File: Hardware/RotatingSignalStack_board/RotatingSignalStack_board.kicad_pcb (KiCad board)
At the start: 2 copper layers, 81.3 x 71.1 mm, 30 parts, among them J1 8P8C_LED_Shielded, J2 Conn_01x05_Pin, SW1 SW_Push, SW2 SW_Push, U1 OKI, U3 Teensy4.1_DEV-16771

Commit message: first layout commit - lots of expected changes
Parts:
- moved R3 32.0 mm to (144.8, 47.0)
- moved R4 32.0 mm to (142.2, 47.0)
- moved C4 17.4 mm to (149.5, 104.1)
- moved C5 17.4 mm to (149.5, 106.7)
- moved C3 17.4 mm to (149.5, 101.6)
- moved U3 7.62 mm to (142.2, 61.0)
- moved J1 6.48 mm to (190.8, 86.9)
- moved C6 3.02 mm to (159.2, 90.2), turned to 180 degrees
- moved R1 2.54 mm to (137.2, 81.3)
- moved D1 2.54 mm to (137.2, 83.8)
- moved J2 2.27 mm to (169.4, 45.7)
- moved Conn5 1.27 mm to (139.7, 74.9)
- moved C1 1.27 mm to (137.2, 87.6)
- moved V2 0.12 mm to (178.9, 49.7)
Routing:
- net +3.3V: track 0.00 -> 145.2 mm, vias 0 -> 4
- net /Tx-: track 0.00 -> 95.0 mm
- net /Tx+: track 0.00 -> 94.8 mm
- net /Rx+: track 0.00 -> 85.0 mm
- net /Rx-: track 0.00 -> 84.8 mm
- net +12V: track 0.00 -> 83.9 mm, vias 0 -> 2
- net /LED: track 0.00 -> 77.1 mm, vias 0 -> 4
- net JOG B: track 0.00 -> 68.6 mm, vias 0 -> 2
- net JOG A: track 0.00 -> 63.6 mm, vias 0 -> 1
- net I2C SCL: track 0.00 -> 54.2 mm, vias 0 -> 1
- net COMP PWR: track 0.00 -> 54.1 mm, vias 0 -> 1
- net I2C SDA: track 0.00 -> 52.6 mm
- net MAG ENABLE: track 0.00 -> 37.7 mm, vias 0 -> 1
- net Net-(C6-Pad1): track 0.00 -> 13.8 mm
- net GND: track 0.00 -> 9.77 mm, vias 0 -> 20
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- added copper zone on B.Cu, net GND
- added copper zone on F.Cu, net GND
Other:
- board size 81.3 x 71.1 mm -> 84.3 x 74.1 mm
- board text added: "COMPASS"
- board text added: "H-BRIDGE"
- board text added: "L"
- board text added: "MOTOR OUT"
- board text added: "PWR IN"
- board text added: "R"
- board text added: "TyTyTheToeH"

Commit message: changes layout reveiw 1
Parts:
- removed Conn5: Molex_SL_04, MRDT_Connectors:MOLEX_SL_04_Vertical
- added Conn1: Molex_SL_03, MRDT_Connectors:MOLEX_SL_03_Vertical, F.Cu at (159.4, 147.6)
- added R5: 0, Jumper:SolderJumper-2_P1.3mm_Open_RoundedPad1.0x1.5mm, B.Cu at (150.2, 104.9)
- Conn2, Conn3: moved to F.Cu
- J2: footprint Connector_PinHeader_1.00mm:PinHeader_1x05_P1.00mm_Vertical -> Connector_PinHeader_2.54mm:PinHeader_1x05_P2.54mm_Vertical
- moved R4 104.9 mm to (165.1, 149.4), turned to 90 degrees
- moved R3 100.4 mm to (165.1, 145.3), turned to 90 degrees
- moved Conn6 93.2 mm to (162.1, 138.9)
- moved J2 88.1 mm to (151.9, 132.1)
- moved SW1 84.6 mm to (178.3, 134.1)
- moved SW2 84.6 mm to (172.2, 134.1)
- moved R13 80.9 mm to (171.7, 140.7)
- moved R18 80.9 mm to (169.2, 140.7)
- moved D14 80.0 mm to (169.2, 144.4), turned to 90 degrees
- moved D13 80.0 mm to (171.7, 144.4), turned to 90 degrees
- moved V1 75.7 mm to (173.7, 91.8), turned to 0 degrees
- moved V2 71.8 mm to (120.6, 91.8), turned to 90 degrees
- moved R1 67.2 mm to (126.2, 147.5)
- moved D1 64.2 mm to (129.9, 147.6), turned to 180 degrees
- moved C1 61.9 mm to (146.4, 148.8), turned to -90 degrees
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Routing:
- net /Rx+: track 85.0 -> 44.4 mm
- net /Rx-: track 84.8 -> 44.3 mm
- net HB_FWD: track 8.98 -> 48.8 mm, vias 0 -> 1
- net /Tx-: track 95.0 -> 55.8 mm
- net /Tx+: track 94.8 -> 55.8 mm
- net HB_RVS: track 8.98 -> 47.3 mm, vias 0 -> 1
- net +12V: track 83.9 -> 54.4 mm
- net COMP PWR: track 54.1 -> 78.4 mm, vias 1 -> 2
- net I2C SCL: track 54.2 -> 78.2 mm, vias 1 -> 3
- net JOG B: track 68.6 -> 45.8 mm, vias 2 -> 1
- net MAG ENABLE: track 37.7 -> 59.2 mm
- net +3.3V: track 145.2 -> 165.1 mm, vias 4 -> 2
- net JOG A: track 63.6 -> 46.1 mm
- net /LED: track 77.1 -> 64.8 mm, vias 4 -> 0
- net I2C SDA: track 52.6 -> 64.1 mm, vias 0 -> 3
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- added copper zone on F.Cu, net +12V
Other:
- board size 84.3 x 74.1 mm -> 69.1 x 69 mm
- board text added: "12v"
- board text added: "3.3v"
- board text added: "3.3v Direct Pwr Compass"
- board text added: "IN"
- board text added: "OUT"
- board text added: "ROTATING SIGNAL STACK"
- board text removed: "MOTOR OUT"
- board text removed: "PWR IN"
- board text removed: "TyTyTheToeH"

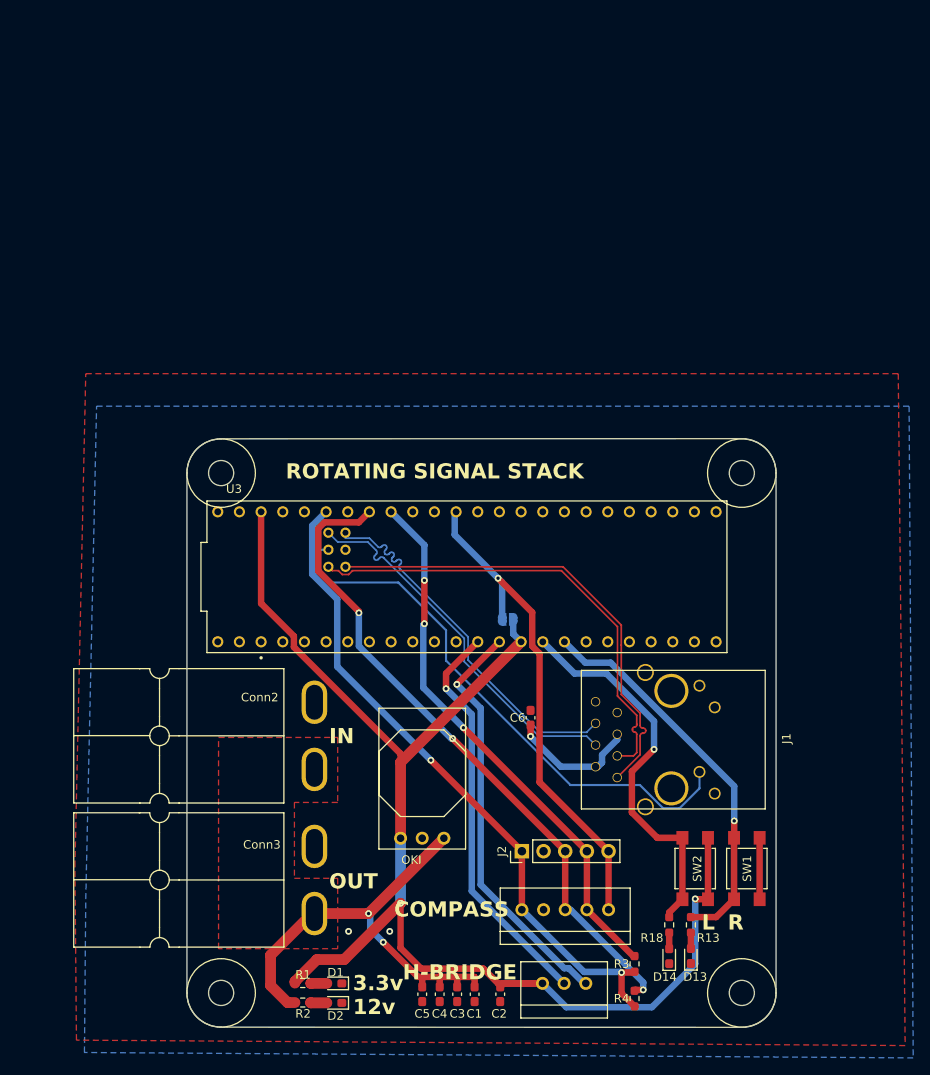
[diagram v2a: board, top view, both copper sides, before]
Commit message: layout changes- diff pair length, moved labels, trace width changed, OKI capacitors moved, x
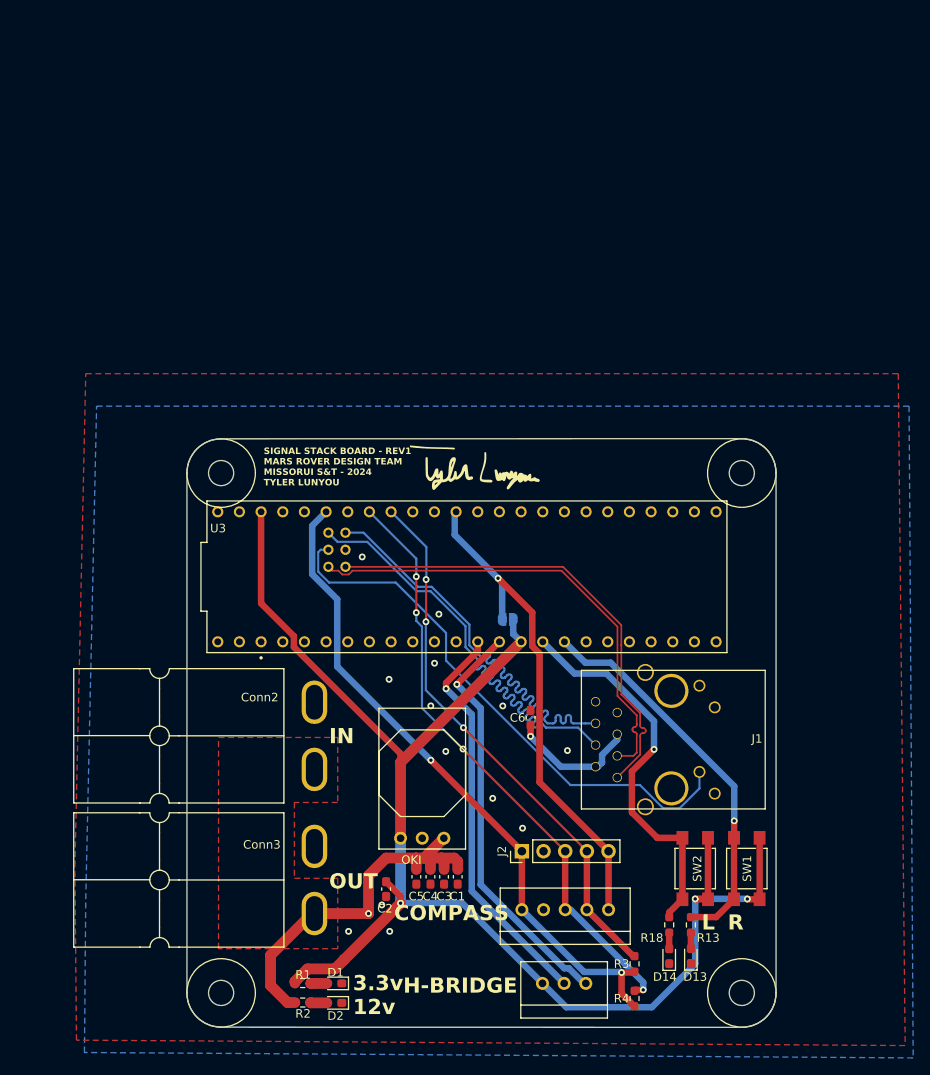
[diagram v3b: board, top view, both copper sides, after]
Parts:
- added G***: LOGO, MRDT_Silkscreens:z_sig_Tyler_Lunyou_Sig_30mmx7, F.Cu at (151.2, 87.1)
- moved C2 18.2 mm to (136.0, 136.5)
- moved C1 13.9 mm to (144.4, 135.1)
- moved C3 13.8 mm to (142.8, 135.1)
- moved C4 13.8 mm to (141.2, 135.1)
- moved C5 13.8 mm to (139.5, 135.1)
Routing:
- net /Rx+: track 44.4 -> 55.4 mm
- net /Rx-: track 44.3 -> 55.4 mm
- net +12V: track 54.4 -> 45.1 mm, vias 2 -> 1
- net I2C SCL: track 78.2 -> 70.8 mm, vias 3 -> 4
- net +3.3V: track 165.1 -> 168.1 mm, vias 2 -> 3
- net GND: vias 2 -> 13
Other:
- board text added: "3.3v Direct Power Compass"
- board text added: "SIGNAL STACK BOARD - REV1 MARS ROVER DESIGN TEAM MISSORUI S&T - 2024 TYLER LUNYOU"
- board text removed: "3.3v Direct Pwr Compass"
- board text removed: "ROTATING SIGNAL STACK"

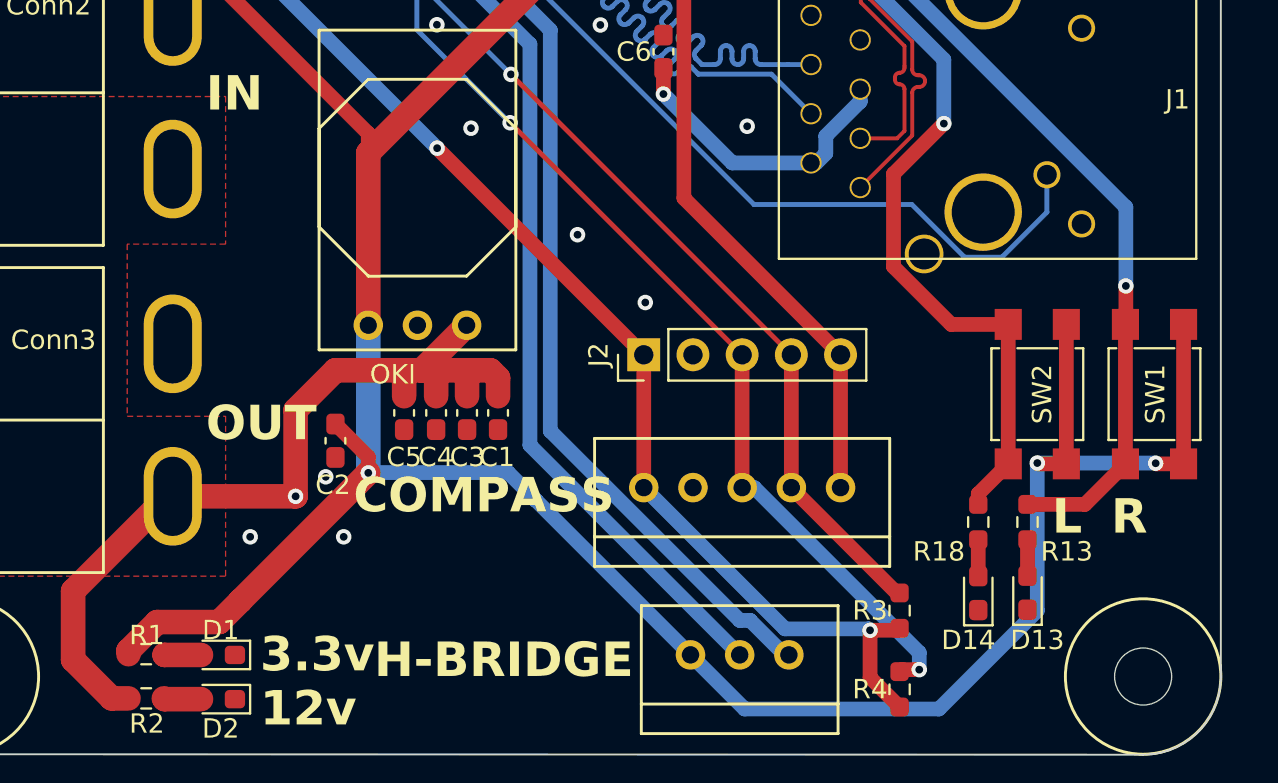
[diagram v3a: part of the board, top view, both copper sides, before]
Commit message: layout changes- diff pair length, moved labels, trace width changed, OKI capacitors moved, x
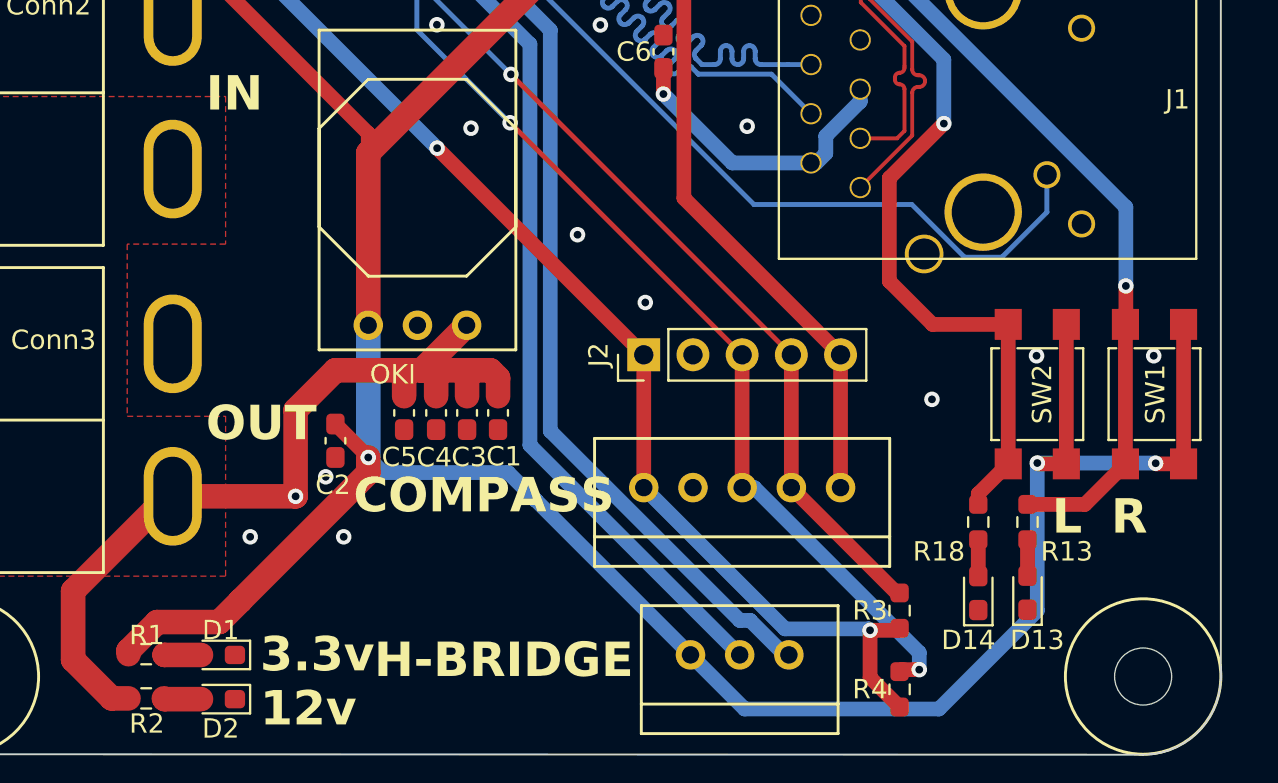
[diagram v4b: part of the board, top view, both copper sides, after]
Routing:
- net JOG B: track 45.8 -> 46.5 mm
- net GND: vias 13 -> 16
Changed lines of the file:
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@@
     (property "ki_keywords" "cap capacitor")
     (attr smd)
-    (fp_text reference "C1" (at 2.286 0.050625 -180) (layer "F.SilkS")
+    (fp_text reference "C1" (at 2.25 -0.30225 -180) (layer "F.SilkS")
         (effects (font (size 1 1) (thickness 0.15)))
     )
@@
     (property "ki_keywords" "cap capacitor")
     (attr smd)
-    (fp_text reference "C4" (at 2.286 0.016875 -180) (layer "F.SilkS")
+    (fp_text reference "C4" (at 2.3 0.1 -180) (layer "F.SilkS")
         (effects (font (size 1 1) (thickness 0.15)))
     )
@@
     (property "ki_keywords" "cap capacitor")
     (attr smd)
-    (fp_text reference "C3" (at 2.286 -0.016875 -180) (layer "F.SilkS")
+    (fp_text reference "C3" (at 2.286 -0.10225 -180) (layer "F.SilkS")
         (effects (font (size 1 1) (thickness 0.15)))
     )
@@
     (property "ki_keywords" "cap capacitor")
     (attr smd)
-    (fp_text reference "C5" (at 2.286 0) (layer "F.SilkS")
+    (fp_text reference "C5" (at 2.286 0.24775) (layer "F.SilkS")
         (effects (font (size 1 1) (thickness 0.15)))
     )
@@
   (via (at 131.572 141.478) (size 0.8) (drill 0.4) (layers "F.Cu" "B.Cu") (free) (net 2))
   (via (at 151.972 129.38) (size 0.8) (drill 0.4) (layers "F.Cu" "B.Cu") (free) (net 2))
+  (via (at 172.172 132.13) (size 0.8) (drill 0.4) (layers "F.Cu" "B.Cu") (free) (net 2))
   (via (at 142.972 120.38) (size 0.8) (drill 0.4) (layers "F.Cu" "B.Cu") (free) (net 2))
   (via (at 149.652 115.05) (size 0.8) (drill 0.4) (layers "F.Cu" "B.Cu") (free) (net 2))
   (via (at 142.162 104.29) (size 0.8) (drill 0.4) (layers "F.Cu" "B.Cu") (free) (net 2))
+  (via (at 166.772 134.38) (size 0.8) (drill 0.4) (layers "F.Cu" "B.Cu") (free) (net 2))
   (via (at 136.322 111.93) (size 0.8) (drill 0.4) (layers "F.Cu" "B.Cu") (free) (net 2))
   (via (at 141.212 115.04) (size 0.8) (drill 0.4) (layers "F.Cu" "B.Cu") (free) (net 2))
@@
   (via (at 148.472 125.88) (size 0.8) (drill 0.4) (layers "F.Cu" "B.Cu") (free) (net 2))
   (via (at 157.232 120.28) (size 0.8) (drill 0.4) (layers "F.Cu" "B.Cu") (free) (net 2))
+  (via (at 178.222 132.13) (size 0.8) (drill 0.4) (layers "F.Cu" "B.Cu") (free) (net 2))
   (segment (start 173.712 130.512) (end 173.712 137.712) (width 0.762) (layer "F.Cu") (net 3))
-  (segment (start 135.972 135.655) (end 137.668 137.351) (width 0.762) (layer "F.Cu") (net 3))
+  (segment (start 125.288 147.358256) (end 125.288 147.5375) (width 1.27) (layer "F.Cu") (net 3))
+  (segment (start 137.668 137.38) (end 137.668 138.176) (width 1.27) (layer "F.Cu") (net 3))
   (segment (start 178.354 137.712) (end 178.322 137.68) (width 0.762) (layer "F.Cu") (net 3))
-  (segment (start 137.668 137.351) (end 137.668 138.176) (width 0.762) (layer "F.Cu") (net 3))
-  (segment (start 129.972 145.88) (end 131.064 144.788) (width 1.27) (layer "F.Cu") (net 3))
+  (segment (start 137.668 137.351) (end 135.972 135.655) (width 0.762) (layer "F.Cu") (net 3))
   (segment (start 179.762 137.712) (end 179.762 130.512) (width 0.762) (layer "F.Cu") (net 3))
+  (segment (start 137.668 138.176) (end 131.064 144.78) (width 1.27) (layer "F.Cu") (net 3))
+  (segment (start 131.064 144.788) (end 129.972 145.88) (width 1.27) (layer "F.Cu") (net 3))
   (segment (start 179.762 137.712) (end 178.354 137.712) (width 0.762) (layer "F.Cu") (net 3))
   (segment (start 173.712 137.712) (end 172.256 137.712) (width 0.762) (layer "F.Cu") (net 3))
-  (segment (start 131.064 144.788) (end 131.064 144.78) (width 1.27) (layer "F.Cu") (net 3))
-  (segment (start 131.064 144.78) (end 137.668 138.176) (width 1.27) (layer "F.Cu") (net 3))
   (segment (start 172.256 137.712) (end 172.212 137.668) (width 0.762) (layer "F.Cu") (net 3))
-  (segment (start 125.288 147.5375) (end 125.288 147.358256) (width 1.27) (layer "F.Cu") (net 3))
   (segment (start 137.668 121.66) (end 151.799 107.529) (width 1.27) (layer "F.Cu") (net 3))
-  (segment (start 126.766256 145.88) (end 129.972 145.88) (width 1.27) (layer "F.Cu") (net 3))
   (segment (start 121.319 92.289) (end 121.319 103.031) (width 0.762) (layer "F.Cu") (net 3))
+  (segment (start 129.972 145.88) (end 126.766256 145.88) (width 1.27) (layer "F.Cu") (net 3))
   (segment (start 125.164 108.146) (end 137.668 120.65) (width 0.762) (layer "F.Cu") (net 3))
   (segment (start 137.668 130.556) (end 137.668 121.66) (width 1.27) (layer "F.Cu") (net 3))
   (segment (start 125.164 106.876) (end 125.164 108.146) (width 0.762) (layer "F.Cu") (net 3))
   (segment (start 137.668 120.65) (end 137.668 121.66) (width 0.762) (layer "F.Cu") (net 3))
-  (segment (start 125.288 147.358256) (end 126.766256 145.88) (width 1.27) (layer "F.Cu") (net 3))
   (segment (start 121.319 103.031) (end 125.164 106.876) (width 0.762) (layer "F.Cu") (net 3))
+  (segment (start 131.064 144.78) (end 131.064 144.788) (width 1.27) (layer "F.Cu") (net 3))
+  (segment (start 137.668 137.38) (end 137.668 137.351) (width 0.762) (layer "F.Cu") (net 3))
+  (segment (start 126.766256 145.88) (end 125.288 147.358256) (width 1.27) (layer "F.Cu") (net 3))
   (via (at 172.212 137.668) (size 0.8) (drill 0.4) (layers "F.Cu" "B.Cu") (net 3))
-  (via (at 137.668 138.176) (size 0.8) (drill 0.4) (layers "F.Cu" "B.Cu") (net 3))
+  (via (at 137.668 137.38) (size 0.8) (drill 0.4) (layers "F.Cu" "B.Cu") (net 3))
   (via (at 178.322 137.68) (size 0.8) (drill 0.4) (layers "F.Cu" "B.Cu") (free) (net 3))
+  (segment (start 137.668 137.38) (end 137.668 130.556) (width 1.27) (layer "B.Cu") (net 3))
   (segment (start 150.876 104.902) (end 150.876 106.606) (width 0.762) (layer "B.Cu") (net 3))
-  (segment (start 146.332 139.6) (end 146.331 139.6) (width 0.762) (layer "B.Cu") (net 3))
+  (segment (start 146.331 139.6) (end 146.332 139.6) (width 0.762) (layer "B.Cu") (net 3))
   (segment (start 150.876 106.606) (end 151.799 107.529) (width 0.762) (layer "B.Cu") (net 3))
-  (segment (start 144.891 138.16) (end 137.684 138.16) (width 0.762) (layer "B.Cu") (net 3))
-  (segment (start 137.684 138.16) (end 137.668 138.176) (width 0.762) (layer "B.Cu") (net 3))
+  (segment (start 137.668 137.38) (end 138.448 138.16) (width 0.762) (layer "B.Cu") (net 3))
+  (segment (start 146.332 139.6) (end 146.332 139.601) (width 0.762) (layer "B.Cu") (net 3))
+  (segment (start 138.448 138.16) (end 144.891 138.16) (width 0.762) (layer "B.Cu") (net 3))
   (segment (start 172.212 145.288) (end 167.132 150.368) (width 0.762) (layer "B.Cu") (net 3))
   (segment (start 178.31 137.668) (end 178.322 137.68) (width 0.762) (layer "B.Cu") (net 3))
   (segment (start 167.132 150.368) (end 157.099 150.368) (width 0.762) (layer "B.Cu") (net 3))
   (segment (start 157.099 150.368) (end 154.305 147.574) (width 0.762) (layer "B.Cu") (net 3))
+  (segment (start 144.891 138.16) (end 146.331 139.6) (width 0.762) (layer "B.Cu") (net 3))
+  (segment (start 146.332 139.601) (end 154.305 147.574) (width 0.762) (layer "B.Cu") (net 3))
   (segment (start 172.212 137.668) (end 172.212 145.288) (width 0.762) (layer "B.Cu") (net 3))
-  (segment (start 137.668 138.176) (end 137.668 130.556) (width 1.27) (layer "B.Cu") (net 3))
-  (segment (start 146.331 139.6) (end 144.891 138.16) (width 0.762) (layer "B.Cu") (net 3))
   (segment (start 172.212 137.668) (end 178.31 137.668) (width 0.762) (layer "B.Cu") (net 3))
-  (segment (start 146.332 139.601) (end 146.332 139.6) (width 0.762) (layer "B.Cu") (net 3))
-  (segment (start 154.305 147.574) (end 146.332 139.601) (width 0.762) (layer "B.Cu") (net 3))
   (segment (start 152.908 118.618) (end 152.908 117.2965) (width 0.762) (layer "F.Cu") (net 4))
   (via (at 152.908 118.618) (size 0.8) (drill 0.4) (layers "F.Cu" "B.Cu") (net 4))
@@
   (segment (start 162.306 109.982) (end 176.784 124.46) (width 0.762) (layer "B.Cu") (net 21))
   (segment (start 176.784 124.46) (end 176.784 128.524) (width 0.762) (layer "B.Cu") (net 21))
-  (segment (start 164.787 122.741) (end 164.787 127.528872) (width 0.762) (layer "F.Cu") (net 22))
-  (segment (start 164.787 127.528872) (end 167.770128 130.512) (width 0.762) (layer "F.Cu") (net 22))
   (segment (start 169.164 139.8035) (end 169.164 139.26) (width 0.762) (layer "F.Cu") (net 22))
-  (segment (start 167.770128 130.512) (end 170.712 130.512) (width 0.762) (layer "F.Cu") (net 22))
+  (segment (start 167.386 120.142) (end 164.572 122.956) (width 0.762) (layer "F.Cu") (net 22))
+  (segment (start 164.572 128.28) (end 166.804 130.512) (width 0.762) (layer "F.Cu") (net 22))
   (segment (start 170.712 137.712) (end 170.712 130.512) (width 0.762) (layer "F.Cu") (net 22))
   (segment (start 169.164 139.26) (end 170.712 137.712) (width 0.762) (layer "F.Cu") (net 22))
-  (segment (start 167.386 120.142) (end 164.787 122.741) (width 0.762) (layer "F.Cu") (net 22))
+  (segment (start 166.804 130.512) (end 170.712 130.512) (width 0.762) (layer "F.Cu") (net 22))
+  (segment (start 164.572 122.956) (end 164.572 128.28) (width 0.762) (layer "F.Cu") (net 22))
   (via (at 167.386 120.142) (size 0.8) (drill 0.4) (layers "F.Cu" "B.Cu") (net 22))
   (segment (start 154.339 107.529) (end 158.062 111.252) (width 0.762) (layer "B.Cu") (net 22))
